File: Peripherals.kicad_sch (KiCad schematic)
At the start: 18 parts, among them J3 1040310811, U5 LSM6DSV, U8 TXB0104RUT

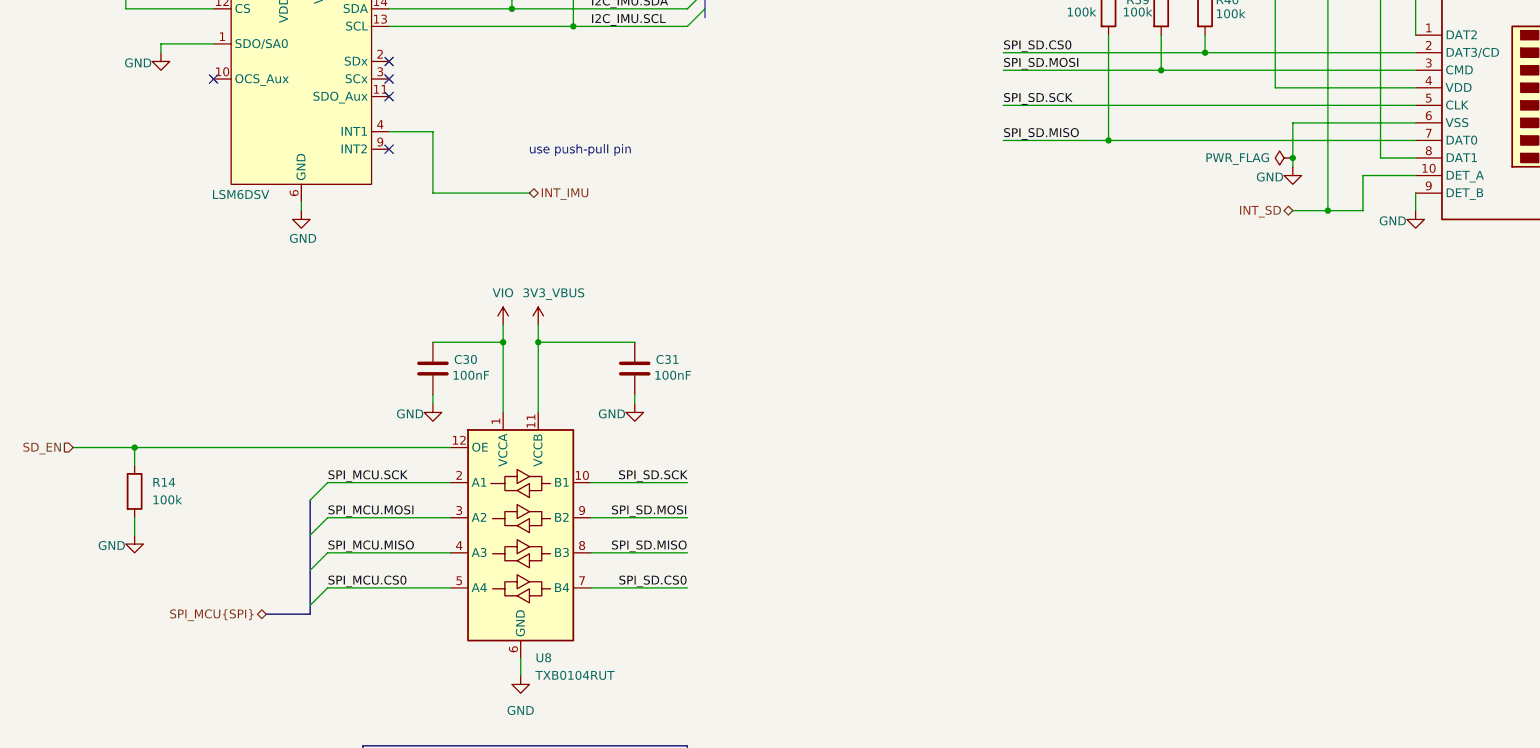
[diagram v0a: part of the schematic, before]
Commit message: new debug connector SOICbite, new board shape, new placement, addition of 22 ohm resistance in fast digital signals as spi
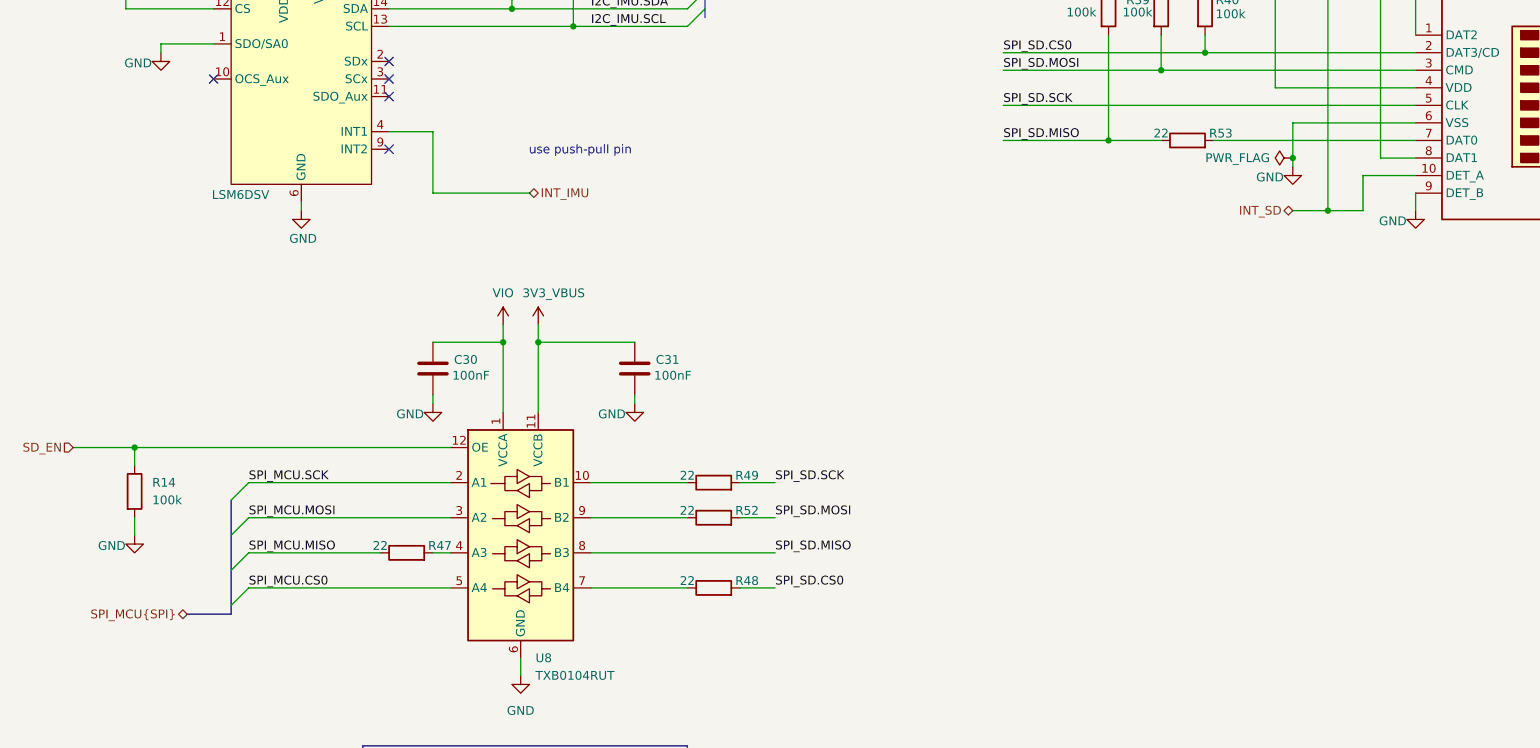
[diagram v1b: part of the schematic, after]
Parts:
- added R47, R48, R49, R52, R53: 22, Resistor_SMD:R_0201_0603Metric, symbol #dzdb:g_res/R-22-0201
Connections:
- net SPI_MCU.MISO: now also R47.1; no longer U8.4 (A3)
- net SPI_SD.CS0: now also R48.2; no longer U8.7 (B4)
- net SPI_SD.MISO: now also R53.1; no longer J3.7 (DAT0)
- net SPI_SD.MOSI: now also R52.2; no longer U8.9 (B2)
- net SPI_SD.SCK: now also R49.2; no longer U8.10 (B1)
- new net: R49.1, U8.10 (B1)
- new net: R52.1, U8.9 (B2)
- new net: J3.7 (DAT0), R53.2
- new net: R47.2, U8.4 (A3)
- new net: R48.1, U8.7 (B4)

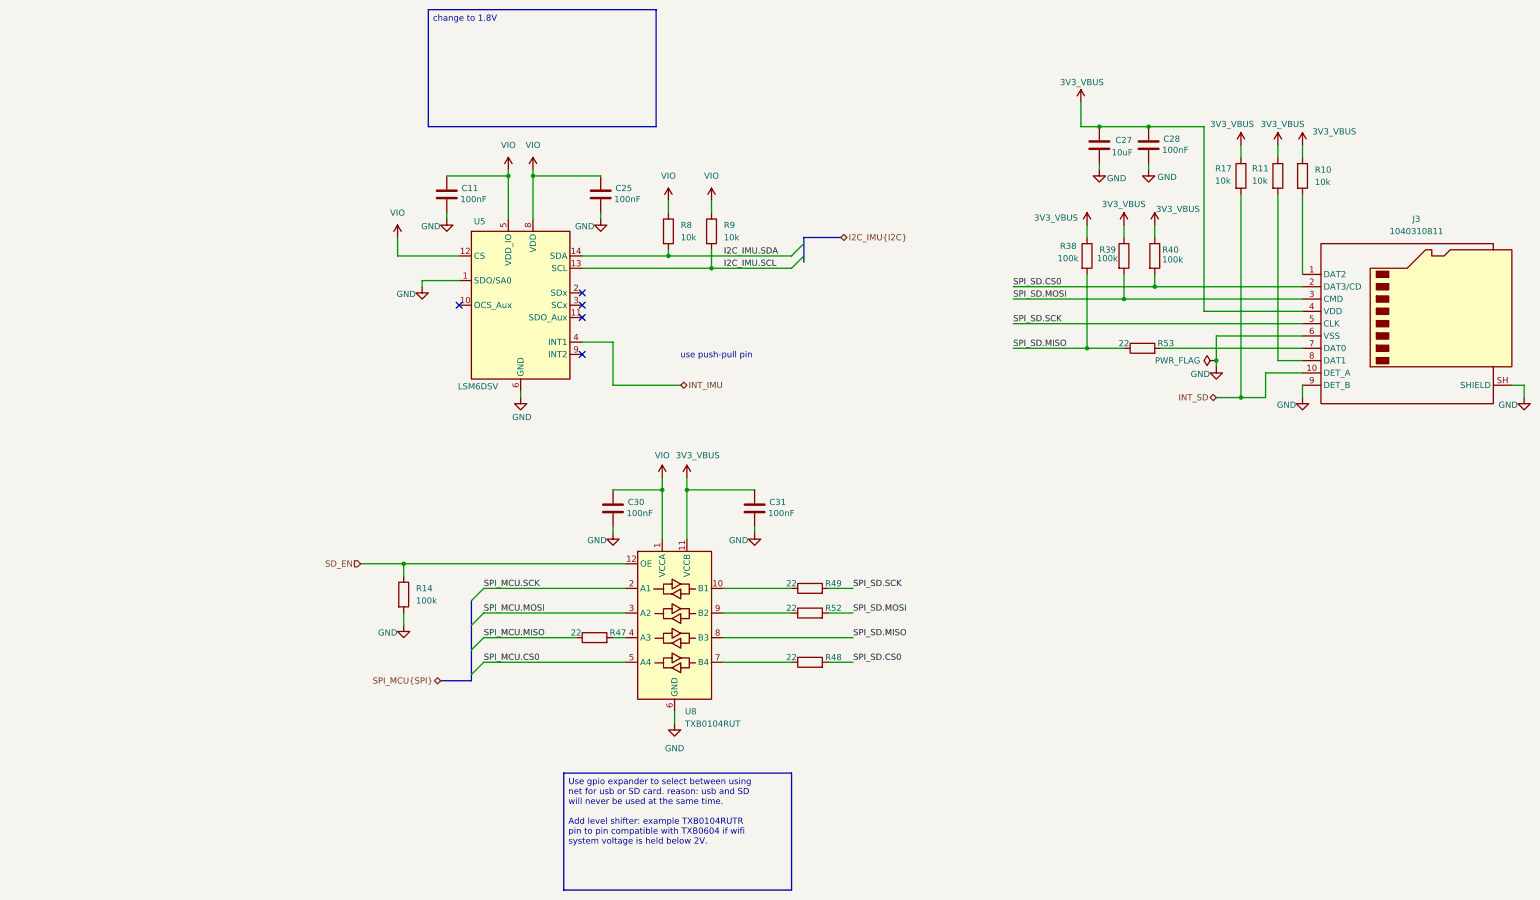
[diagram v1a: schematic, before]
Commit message: initial routing of SPI, USB and Power
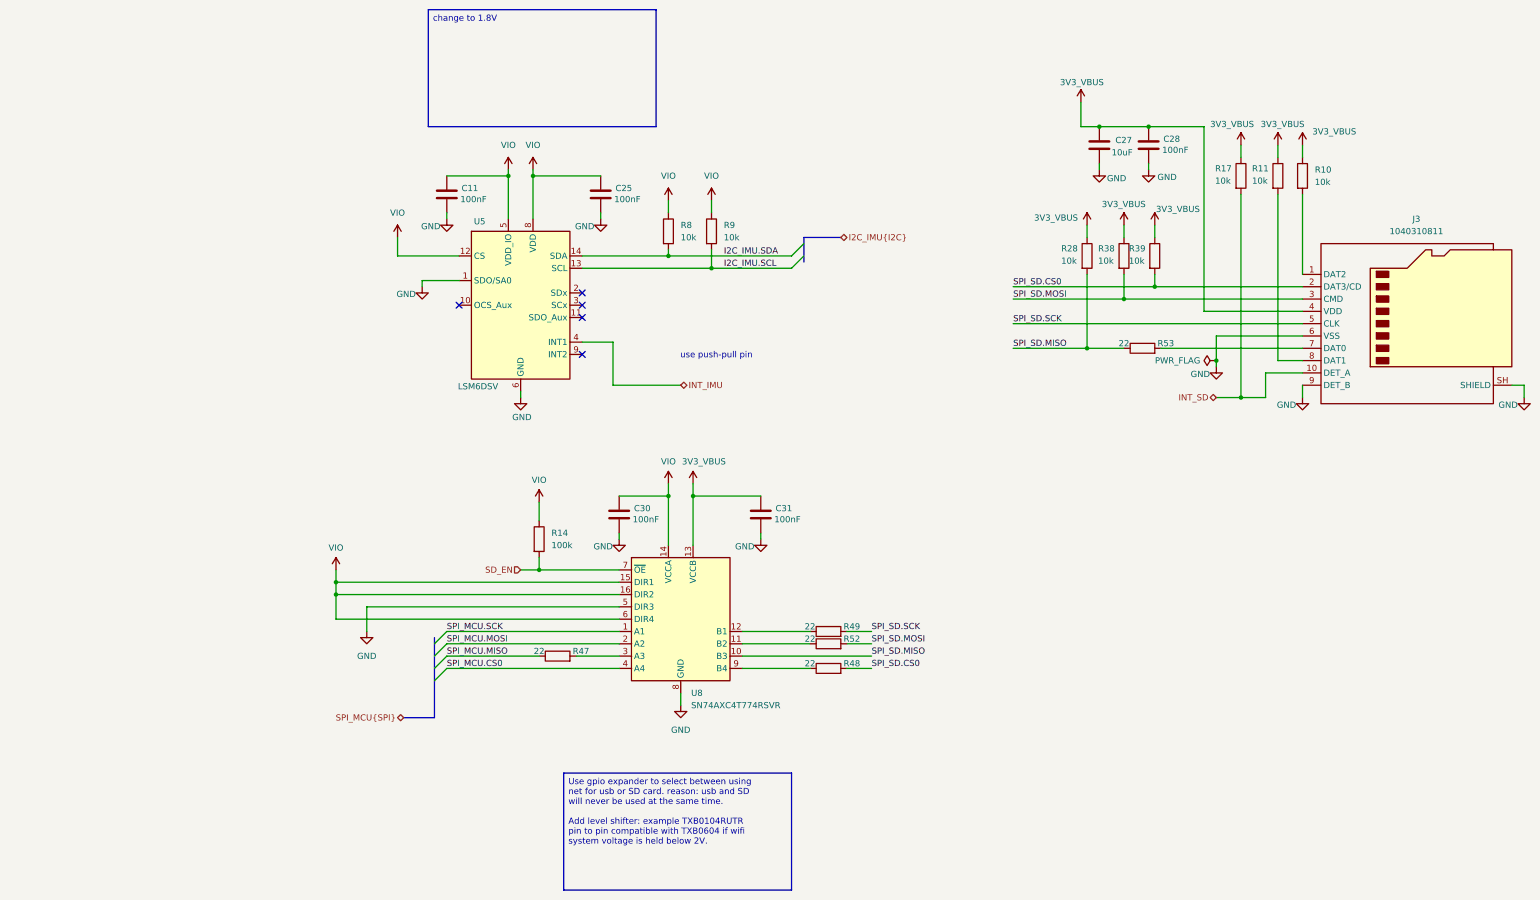
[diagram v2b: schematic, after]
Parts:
- removed R38, R39, R40: 100k, Resistor_SMD:R_0402_1005Metric, symbol #dzdb:g_res/R-100k-0402
- removed U8: TXB0104RUT, Package_DFN_QFN:Texas_R-PUQFN-N12, symbol Logic_LevelTranslator:TXB0104RUT
- added R28, R38, R39: 10k, Resistor_SMD:R_0402_1005Metric, symbol #dzdb:g_res/R-10k-0402
- added U8: SN74AXC4T774RSVR, Package_DFN_QFN:UQFN-16_1.8x2.6mm_P0.4mm, symbol #dzdb:s_comm/COMM-TI-SN74AXC4T774RSVR
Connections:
- net 3V3_VBUS: now also R28.1, R38.1, R39.1, U8.13 (VCCB)
- net GND: now also U8.5 (DIR3), U8.8 (GND); no longer R14.2
- net SD_EN: now also R14.2, U8.7 (~{OE}); no longer R14.1
- net SPI_MCU.CS0: now also U8.4 (A4)
- net SPI_MCU.MOSI: now also U8.2 (A2)
- net SPI_MCU.SCK: now also U8.1 (A1)
- net SPI_SD.CS0: now also R39.2
- net SPI_SD.MISO: now also R28.2, U8.10 (B3)
- net SPI_SD.MOSI: now also R38.2
- net VIO: now also R14.1, U8.14 (VCCA), U8.15 (DIR1), U8.16 (DIR2), U8.6 (DIR4)
- net at R49.1: now also U8.12 (B1)
- net at R52.1: now also U8.11 (B2)
- net at R47.2: now also U8.3 (A3)
- net at R48.1: now also U8.9 (B4)
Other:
- moved on the sheet: C30, C31, R14, R47, R48, R49, R52

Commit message: Comments on layout
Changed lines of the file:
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@@
+		)
+	)
+	(text_box "change all 100 nf caps to 0201 size"
+		(exclude_from_sim no)
+		(at 59.69 97.79 0)
+		(size 82.55 24.13)
+		(margins 0.9525 0.9525 0.9525 0.9525)
+		(stroke
+			(width 0)
+			(type solid)
+		)
+		(fill
+			(type color)
+			(color 255 153 0 1)
+		)
+		(effects
+			(font
+				(size 1.27 1.27)
+			)
+			(justify left top)
 		)
 	)

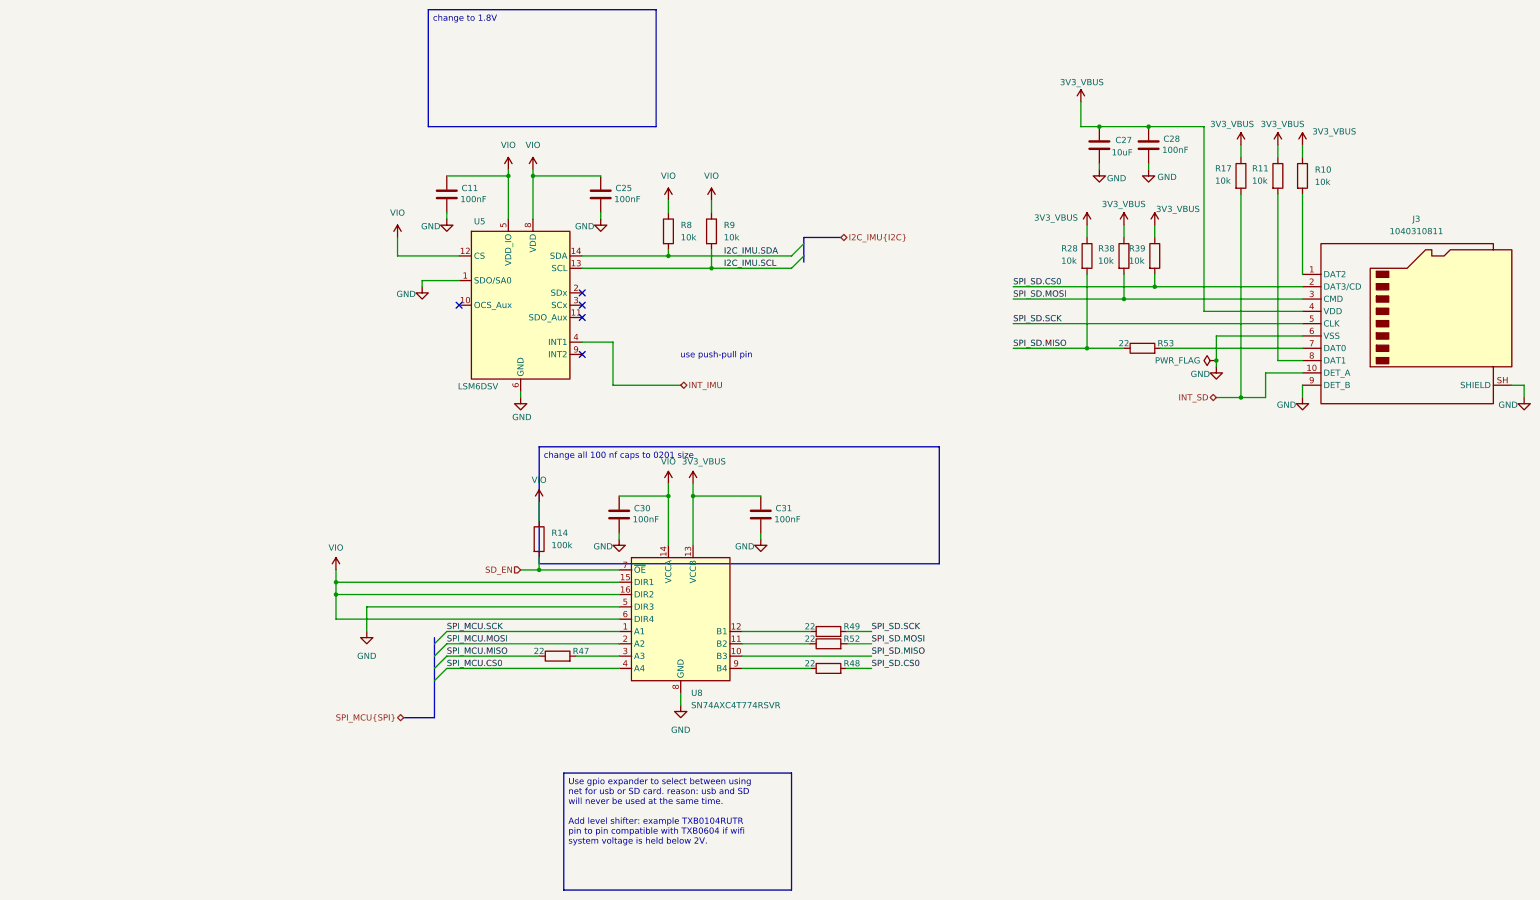
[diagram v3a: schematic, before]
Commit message: updated routing SPI, change 0402 to 0201
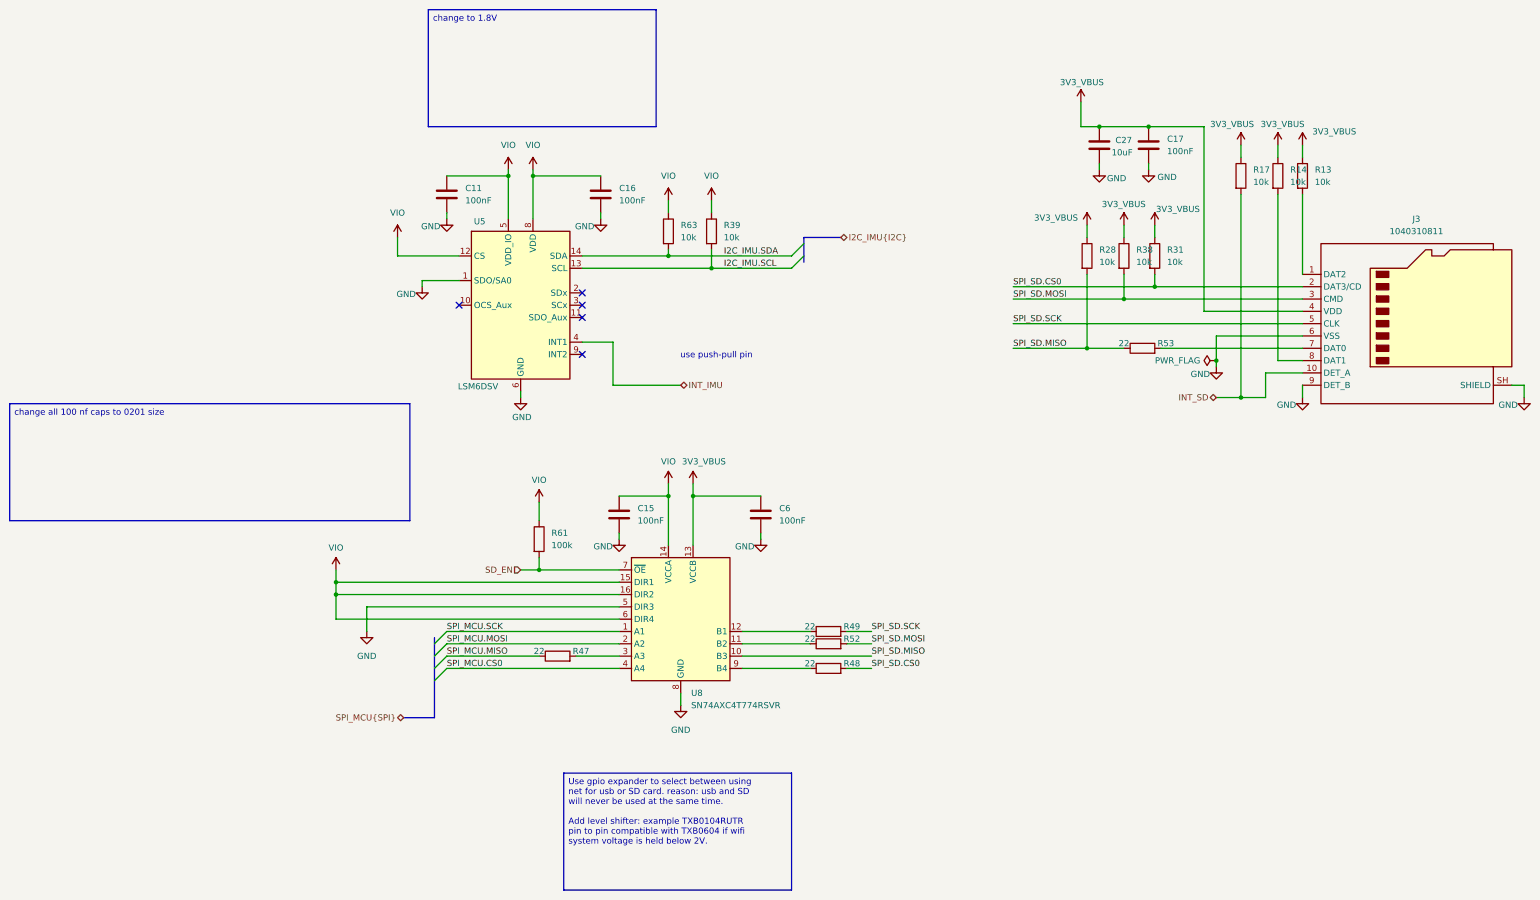
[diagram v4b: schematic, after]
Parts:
- removed C11, C25, C28, C30, C31: 100nF, Capacitor_SMD:C_0603_1608Metric, symbol #dzdb:g_cap/C-100n-0603
- removed R10, R11, R17, R28, R38, R39, R8, R9: 10k, Resistor_SMD:R_0402_1005Metric, symbol #dzdb:g_res/R-10k-0402
- removed R14: 100k, Resistor_SMD:R_0402_1005Metric, symbol #dzdb:g_res/R-100k-0402
- added C11, C15, C16, C17, C6: 100nF, Capacitor_SMD:C_0201_0603Metric, symbol #dzdb:g_cap/C-100n-0201
- added R13, R14, R17, R28, R31, R38, R39, R63: 10k, Resistor_SMD:R_0201_0603Metric, symbol #dzdb:g_res/R-10K-0201
- added R61: 100k, Resistor_SMD:R_0201_0603Metric, symbol #dzdb:g_res/R-100K-0201
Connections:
- net 3V3_VBUS: now also C17.1, C6.1, R13.1, R14.1, R17.1, R28.1, R31.1, R38.1
- net GND: now also C11.2, C15.2, C16.2, C17.2, C6.2
- net I2C_IMU.SCL: now also R39.2
- net I2C_IMU.SDA: now also R63.2
- net INT_SD: now also R17.2
- net SD_EN: now also R61.2
- net SPI_SD.CS0: now also R31.2
- net SPI_SD.MISO: now also R28.2
- net SPI_SD.MOSI: now also R38.2
- net VIO: now also C11.1, C15.1, C16.1, R39.1, R61.1, R63.1
- net at J3.1 (DAT2): now also R13.2
- net at J3.8 (DAT1): now also R14.2
